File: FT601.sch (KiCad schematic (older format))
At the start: 23 parts, among them U1 FT601, U2 ESD7016, U4 ECP5, U5 Si5351, X1 GSB443133HR, Y1 FL3000027, Y2 ABM11-141-26.000MHZ

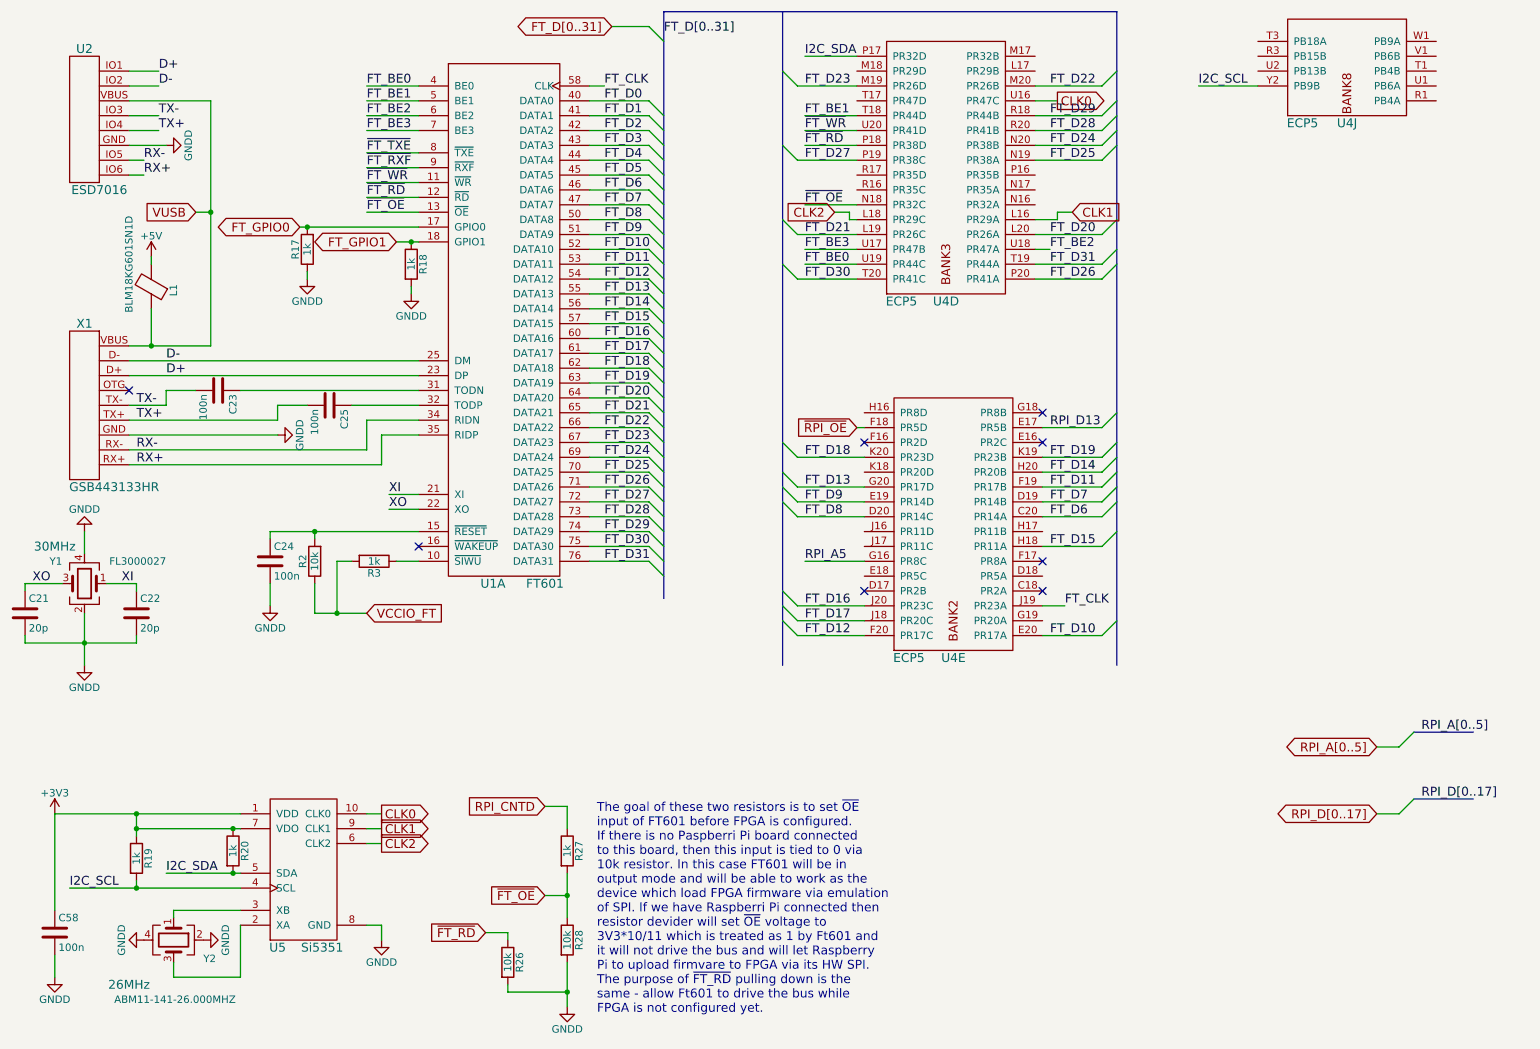
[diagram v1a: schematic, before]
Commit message: Fix bug with not traced FT_TXE FT_RXF
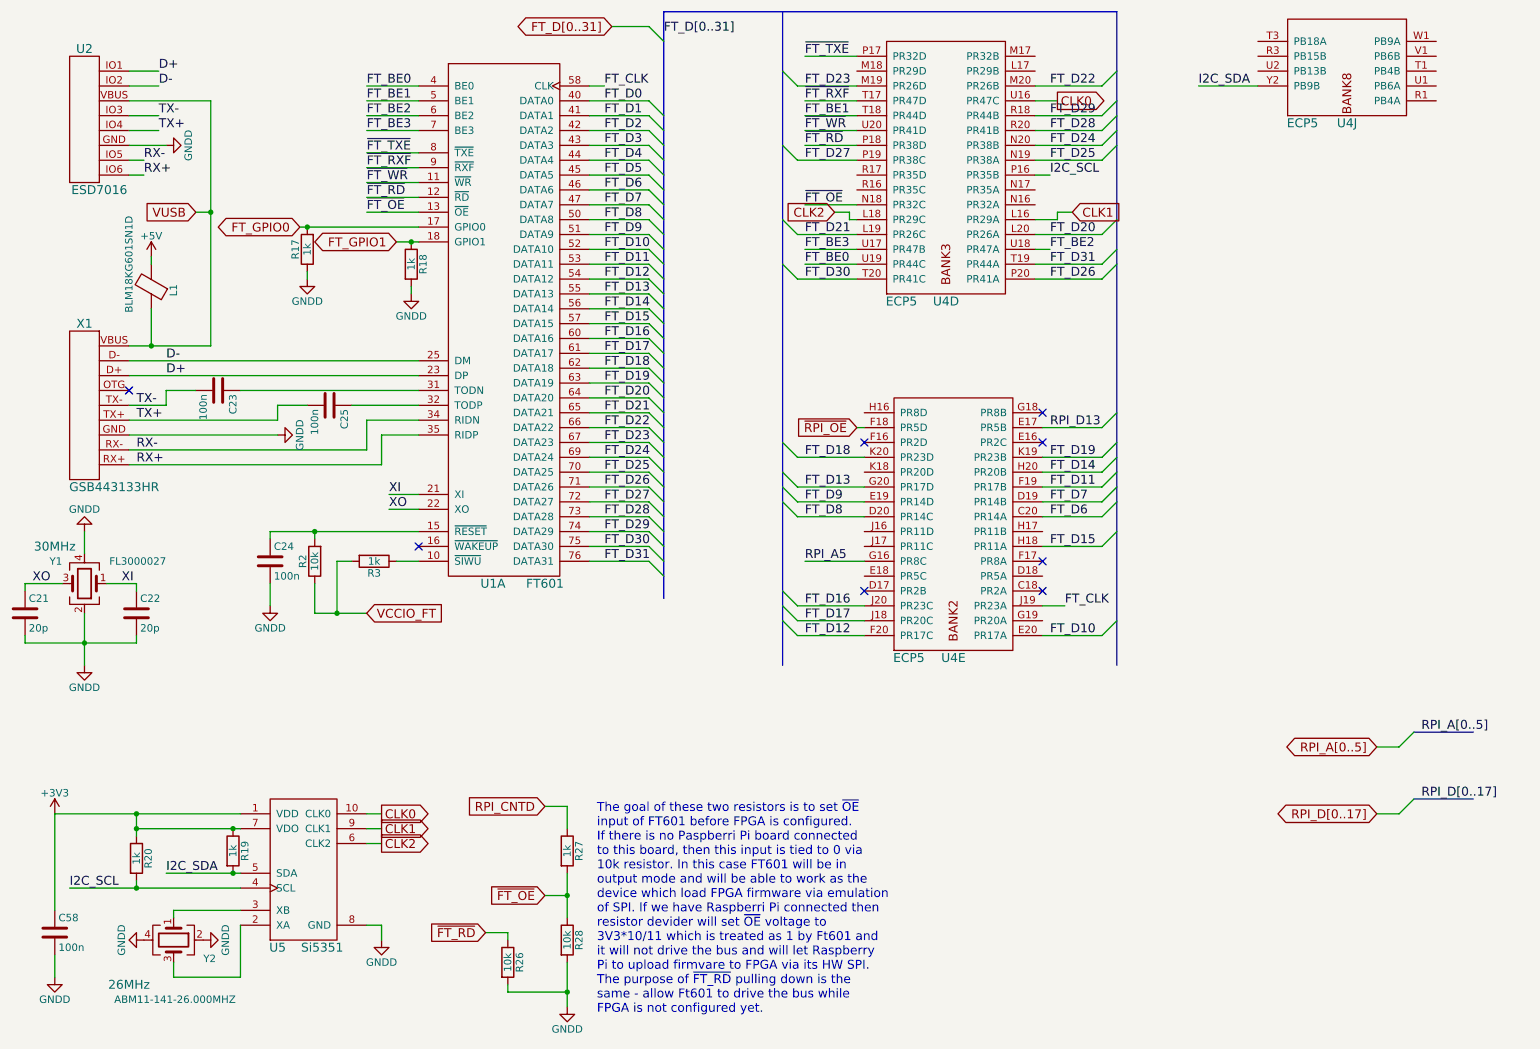
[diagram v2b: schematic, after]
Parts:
- renumbered R20 to R19, R19 to R20
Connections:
- net I2C_SCL: now also U4.P16 (PR35B); no longer U4.Y2 (PB9B)
- net I2C_SDA: now also U4.Y2 (PB9B); no longer U4.P17 (PR32D)
- net ~FT_RXF: now also U4.T17 (PR47D)
- net ~FT_TXE: now also U4.P17 (PR32D)
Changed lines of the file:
@@
 $EndComp
 $Comp
-L R R20
+L R R19
 U 1 1 58A3F9FE
 P 2250 6450
-F 0 "R20" V 2330 6450 50  0000 C CNN
+F 0 "R19" V 2330 6450 50  0000 C CNN
 F 1 "1k" V 2250 6450 50  0000 C CNN
 F 2 "Resistors_SMD:R_0603" V 2180 6450 50  0001 C CNN
@@
 $EndComp
 $Comp
-L R R19
+L R R20
 U 1 1 58A4018A
 P 1600 6500
-F 0 "R19" V 1680 6500 50  0000 C CNN
+F 0 "R20" V 1680 6500 50  0000 C CNN
 F 1 "1k" V 1600 6500 50  0000 C CNN
 F 2 "Resistors_SMD:R_0603" V 1530 6500 50  0001 C CNN
@@
 Text Label 1150 6700 0    60   ~ 0
 I2C_SCL
-Text Label 6100 1100 0    60   ~ 0
+Text Label 8750 1300 0    60   ~ 0
 I2C_SDA
-Text Label 8750 1300 0    60   ~ 0
+Text Label 7750 1900 0    60   ~ 0
 I2C_SCL
 Wire Wire Line
@@
 Wire Wire Line
 	9150 1300 8750 1300
+Wire Wire Line
+	7750 1900 7650 1900
+Text Label 6100 1100 0    60   ~ 0
+~FT_TXE
+Text Label 6100 1400 0    60   ~ 0
+~FT_RXF
+Wire Wire Line
+	6450 1400 6100 1400
 $EndSCHEMATC

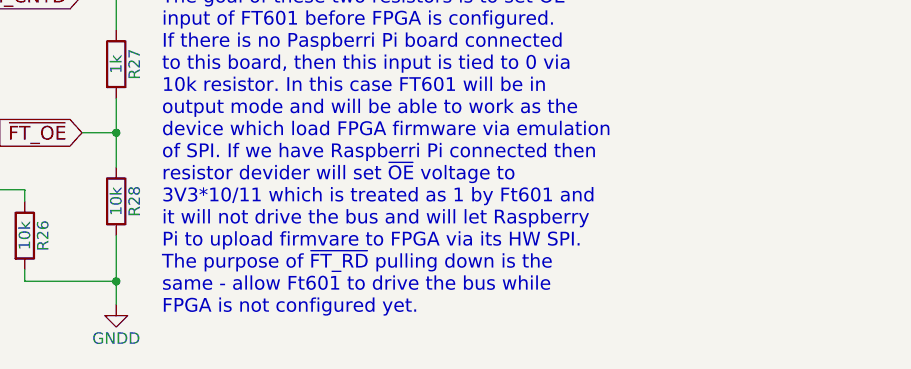
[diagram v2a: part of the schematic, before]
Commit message: Finish tracing all except SDRAM and AFE
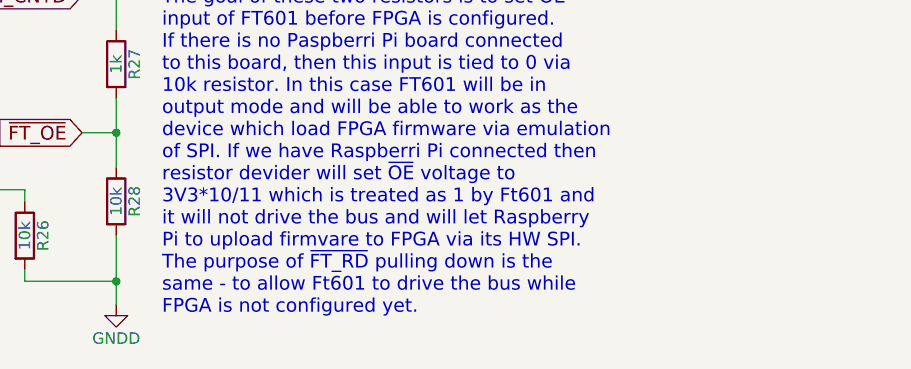
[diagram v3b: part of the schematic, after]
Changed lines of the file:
@@
 Connection ~ 4500 6750
 Text Notes 4700 7550 0    60   ~ 0
-The goal of these two resistors is to set ~OE~\ninput of FT601 before FPGA is configured.\nIf there is no Paspberri Pi board connected\nto this board, then this input is tied to 0 via\n10k resistor. In this case FT601 will be in\noutput mode and will be able to work as the\ndevice which load FPGA firmware via emulation\nof SPI. If we have Raspberri Pi connected then \nresistor devider will set ~OE~ voltage to\n3V3*10/11 which is treated as 1 by Ft601 and\nit will not drive the bus and will let Raspberry\nPi to upload firmvare to FPGA via its HW SPI.\nThe purpose of ~FT_RD~ pulling down is the \nsame - allow Ft601 to drive the bus while \nFPGA is not configured yet.
+The goal of these two resistors is to set ~OE~\ninput of FT601 before FPGA is configured.\nIf there is no Paspberri Pi board connected\nto this board, then this input is tied to 0 via\n10k resistor. In this case FT601 will be in\noutput mode and will be able to work as the\ndevice which load FPGA firmware via emulation\nof SPI. If we have Raspberri Pi connected then \nresistor devider will set ~OE~ voltage to\n3V3*10/11 which is treated as 1 by Ft601 and\nit will not drive the bus and will let Raspberry\nPi to upload firmvare to FPGA via its HW SPI.\nThe purpose of ~FT_RD~ pulling down is the \nsame - to allow Ft601 to drive the bus while \nFPGA is not configured yet.
 Text GLabel 3950 7000 0    60   Input ~ 0
 ~FT_RD
